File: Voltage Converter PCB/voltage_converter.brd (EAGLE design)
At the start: 22.5 x 29.2 mm, 11 parts

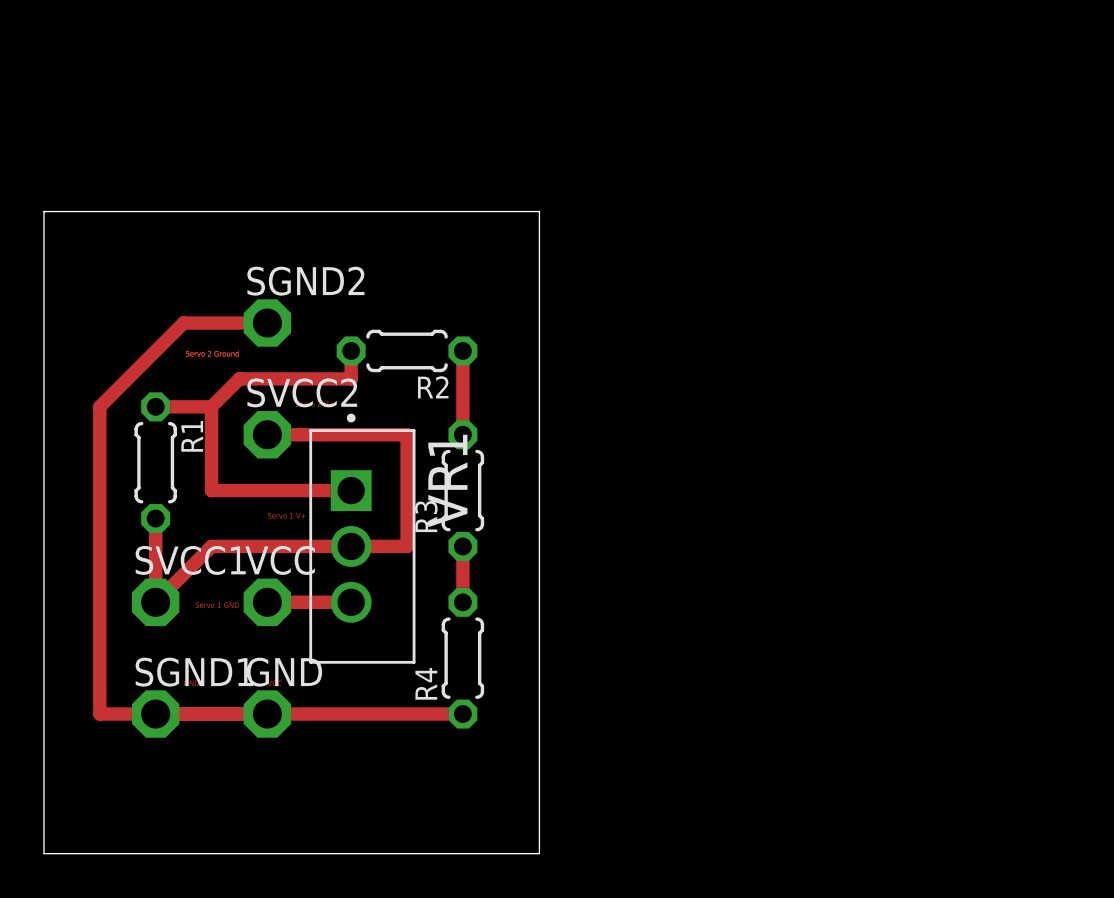
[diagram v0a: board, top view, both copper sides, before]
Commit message: consolidated facial detection, added battery_basket, new voltage converter board
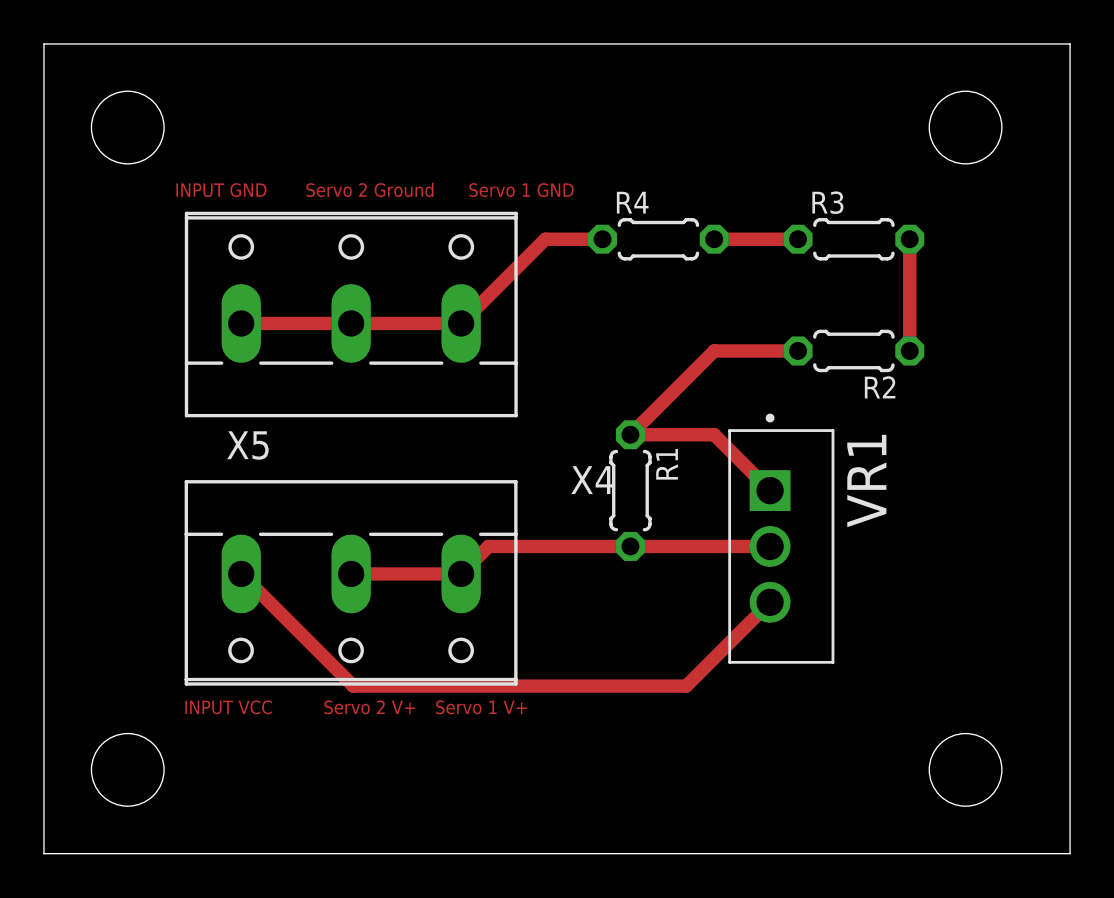
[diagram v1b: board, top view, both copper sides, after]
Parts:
- removed GND, SGND1, SGND2, SVCC1, SVCC2, VCC: TPPAD1-13, testpad:P1-13
- added X4, X5: (no value), con-wago-500:W237-103
- moved R1 21.6 mm to (26.7, 16.5)
- moved R3 21.1 mm to (36.8, 27.9), turned to 0 degrees
- moved R4 21.0 mm to (27.9, 27.9), turned to 0 degrees
- moved R2 20.3 mm to (36.8, 22.9)
- moved VR1 19.1 mm to (33.0, 14.0)
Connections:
- net +8V: now also X4.1, X4.2; no longer SVCC1.TP, SVCC2.TP
- net GND: now also X5.1, X5.2, X5.3; no longer GND.TP, SGND1.TP, SGND2.TP
- net VCC: now also X4.3; no longer VCC.TP
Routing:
- net GND: track 44.8 -> 18.0 mm
- net VCC: track 3.81 -> 27.7 mm
- net +8V: track 27.7 -> 19.6 mm
- net N$3: track 20.8 -> 16.6 mm
- net N$2: track 3.81 -> 5.08 mm
- net N$1: track 2.54 -> 3.81 mm
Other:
- board size 22.5 x 29.2 mm -> 46.7 x 36.8 mm
- board text added: "INPUT GND"
- board text added: "INPUT VCC"
- board text removed: "GND"
- board text removed: "VCC"
